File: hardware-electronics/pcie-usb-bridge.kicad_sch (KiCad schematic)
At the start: 18 parts, among them U3 PI7C9X440SLBFDE, Y1 ABM8-12.000MHZ-B2-T

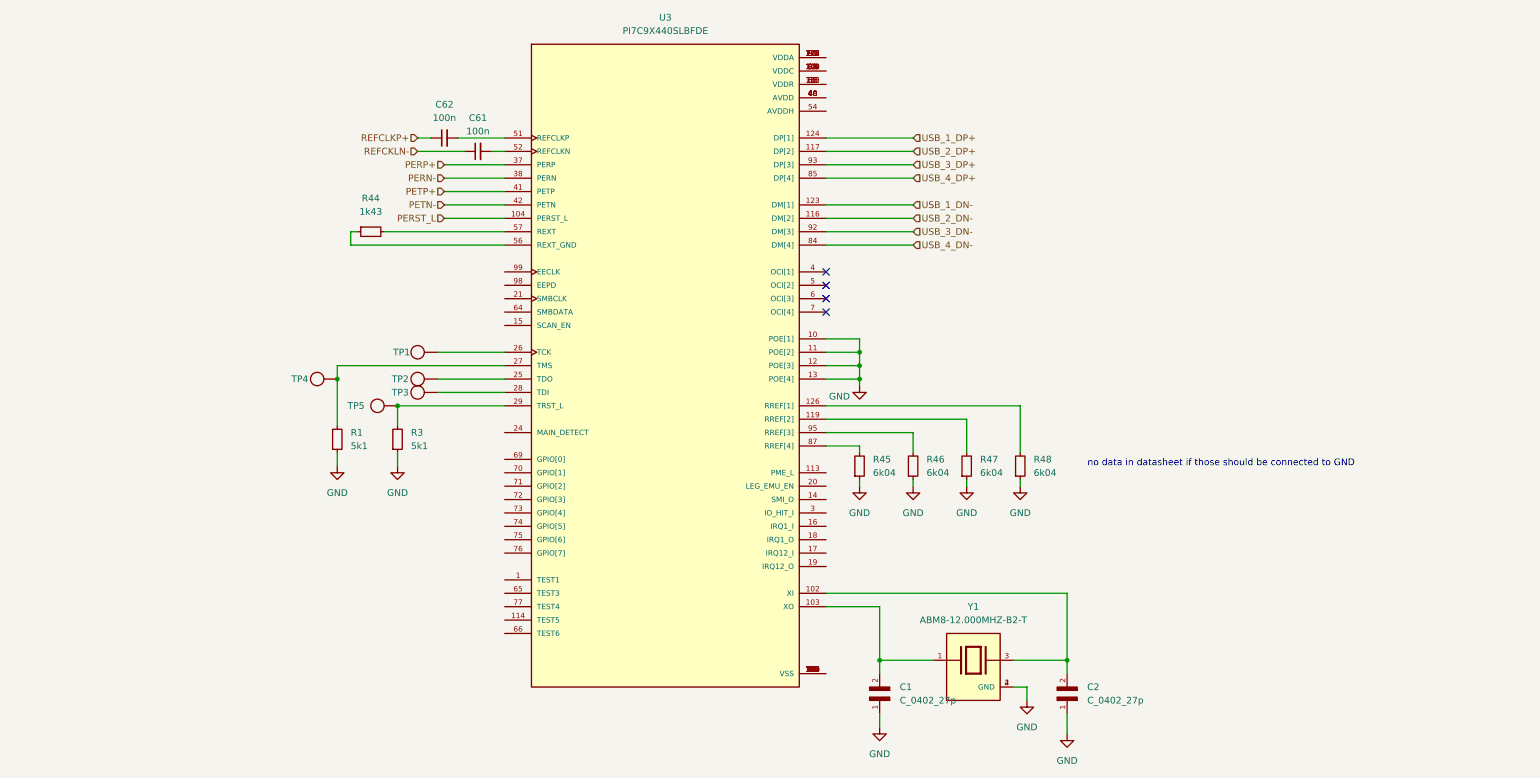
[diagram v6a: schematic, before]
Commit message: [#8] SCH PCIe to USB Connect power pins
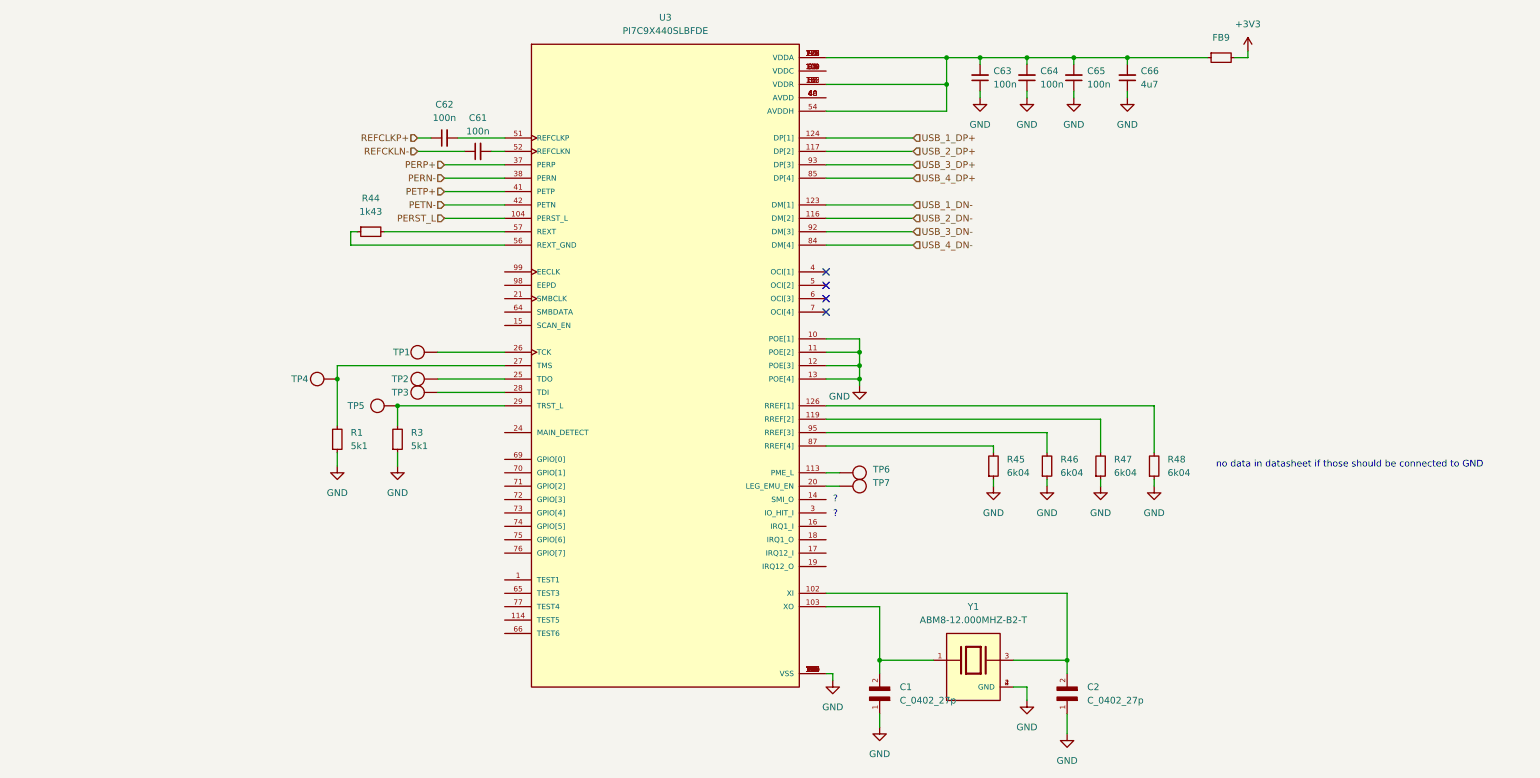
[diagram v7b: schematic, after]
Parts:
- added C63, C64, C65: C_100n_0402, M2SmartHomeFootprints:C_0402, symbol M2SmartHomeSymbols:C_100n_0402
- added C66: C_4u7_0402, M2SmartHomeFootprints:C_0402, symbol M2SmartHomeSymbols:C_4u7_0402
- added FB9: FB_120R_0603, M2SmartHomeFootprints:FB_0603, symbol M2SmartHomeSymbols:FB_120R_0603
- added TP6, TP7: ~, symbol M2SmartHomeSymbols:TP_SMD_1mm
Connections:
- net GND: now also U3.101 (VSS), U3.106 (VSS), U3.110 (VSS), U3.118 (VSS), U3.120 (VSS), U3.125 (VSS), U3.127 (VSS), U3.129 (VSS), U3.23 (VSS), U3.34 (VSS), U3.36 (VSS), U3.39 (VSS), U3.45 (VSS), U3.50 (VSS), U3.53 (VSS), U3.61 (VSS), U3.68 (VSS), U3.82 (VSS), U3.86 (VSS), U3.89 (VSS), U3.9 (VSS), U3.94 (VSS), U3.96 (VSS), C63.1, C64.1, C65.1, C66.1
- net at U3.105 (VDDR), U3.112 (VDDR), U3.33 (VDDR)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: now also U3.115 (VDDA), U3.121 (VDDA), U3.122 (VDDA), U3.128 (VDDA), U3.54 (AVDDH), U3.83 (VDDA), U3.90 (VDDA), U3.91 (VDDA), U3.97 (VDDA), C63.2, C64.2, C65.2, C66.2, FB9.1
- net at U3.113 (PME_L): now also TP6.
- net at U3.20 (LEG_EMU_EN): now also TP7.
- new net +3V3: FB9.2
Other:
- note added: "?"
- moved on the sheet: R45, R46, R47, R48

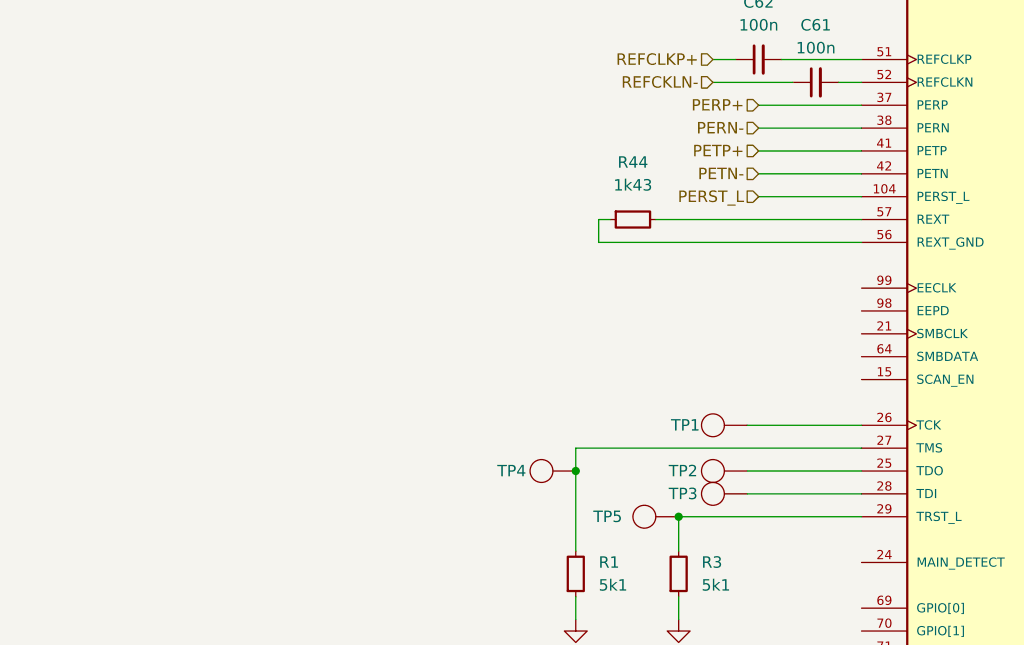
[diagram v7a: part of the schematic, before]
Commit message: [#8] SCH PCIe to USB Connected EEPROM
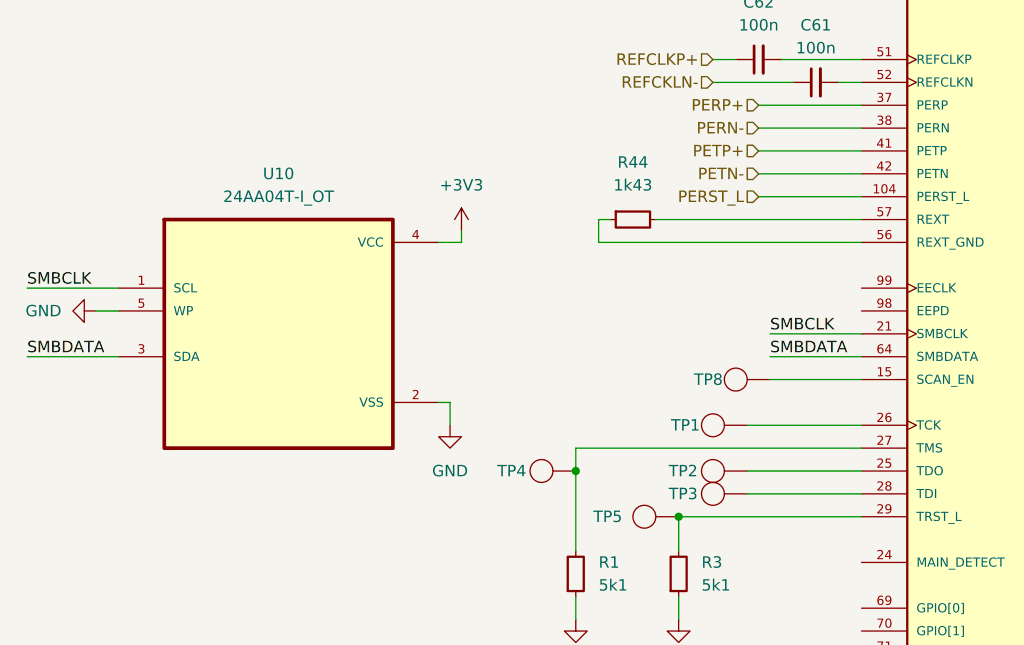
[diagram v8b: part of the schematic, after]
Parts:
- added TP8: ~, symbol M2SmartHomeSymbols:TP_SMD_1mm
- added U10: 24AA04T-I_OT, M2SmartHomeFootprints:24AA04T-I_OT, symbol M2SmartHomeSymbols:24AA04T-I_OT
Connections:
- net +3V3: now also U10.4 (VCC)
- net GND: now also U10.2 (VSS), U10.5 (WP)
- net at U3.15 (SCAN_EN): now also TP8.
- net SMBCLK: now reaches U3.21 (SMBCLK)
- net SMBCLK: now also U10.1 (SCL)
- net SMBDATA: now reaches U3.64 (SMBDATA)
- net SMBDATA: now also U10.3 (SDA)
